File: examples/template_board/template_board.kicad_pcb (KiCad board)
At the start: 2 copper layers, 109.3 x 58.3 mm, 19 parts, among them U101 TPS560430YF

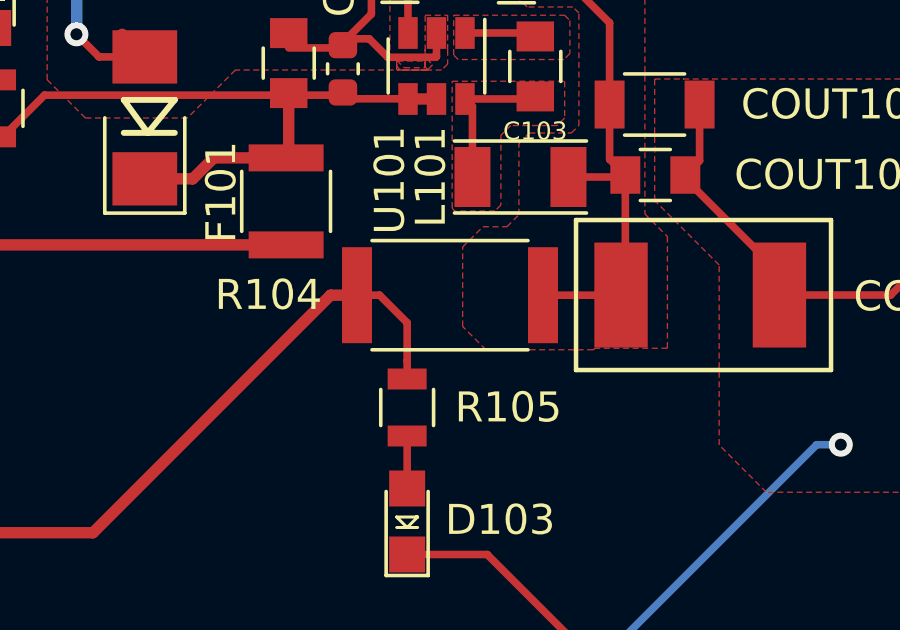
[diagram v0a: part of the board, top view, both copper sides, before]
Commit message: fix: update footprint for 100H inductor (#118)
fix: update layout to match schematic of buck converter

Co-authored-by: Melissa Kazazić <mkazazic01@gmail.com>
Co-authored-by: drewnotdrew <53927275+drewnotdrew@users.noreply.github.com>

Co-authored-by: Melissa Kazazić <mkazazic01@gmail.com>
Co-authored-by: drewnotdrew <53927275+drewnotdrew@users.noreply.github.com>
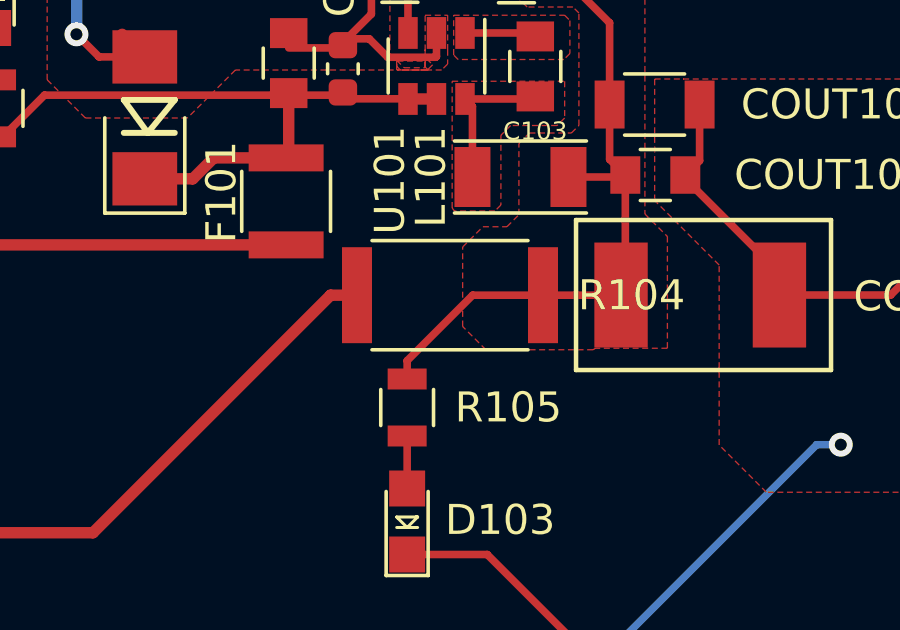
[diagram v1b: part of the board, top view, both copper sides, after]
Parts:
- turned R104 to 0 degrees
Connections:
- net /12V renamed +BATT
- R104 pad 1: Net-(COUT101-Pad1) -> +5V
- R104 pad 2: VCC -> Net-(COUT101-Pad1)
- R105 pad 1: VCC -> Net-(COUT101-Pad1)
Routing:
- net VCC: track 22.7 -> 0.00 mm
- net +5V: track 0.00 -> 18.8 mm
- net Net-(COUT101-Pad1): track 17.3 -> 23.3 mm

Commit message: KiCad 6 :tada: :tada: :tada:  (#151)
* chore: migrate parts library to kicad 6

* feat: switch kibot to kicad 6

* chore: migrate projects to kicad 6

* chore: remove legacy files

* chore: remove legacy cache.lib

* chore: remove rescue libraries

* fix: correct 3D model paths where possible

* chore: annotate migrated schematics

* feat: remove legacy project filter

* fix(bazel): update config for new project structure

* fix(git): unignore external interface

* fix: misc tweaks to resolve kibot errors
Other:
- net class Default removed
